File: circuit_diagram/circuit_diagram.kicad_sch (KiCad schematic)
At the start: 8 parts, among them J1 GPIO, J2 OLED_I2C_display, SW1 Hall_Effect_Flow_Switch, U1 MCP3008, U2 40PC250G

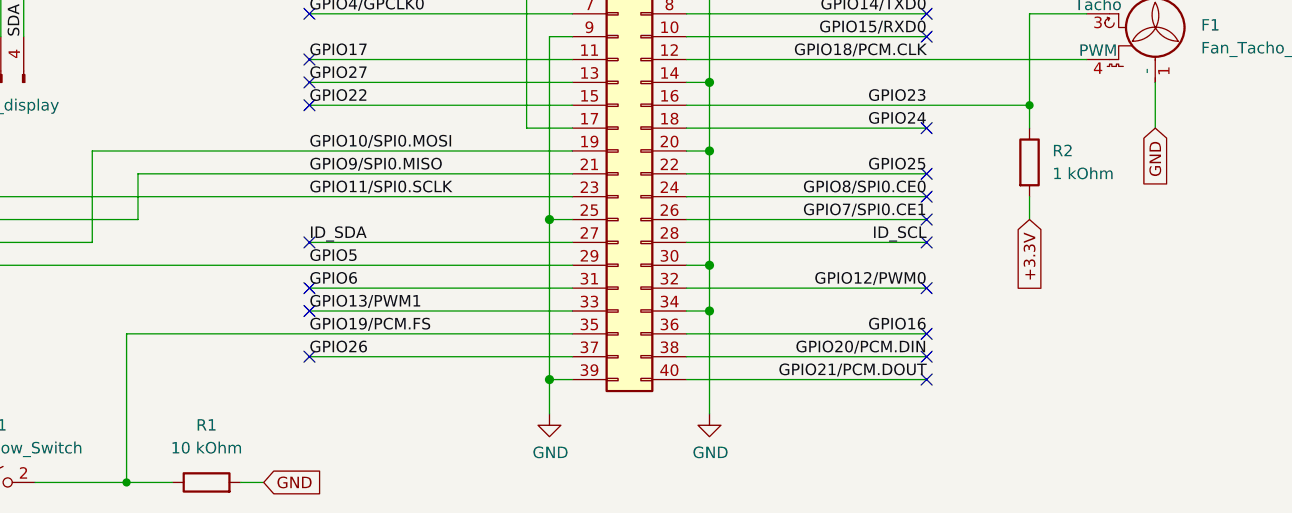
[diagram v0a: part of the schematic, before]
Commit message: Change to kΩ from kOhm
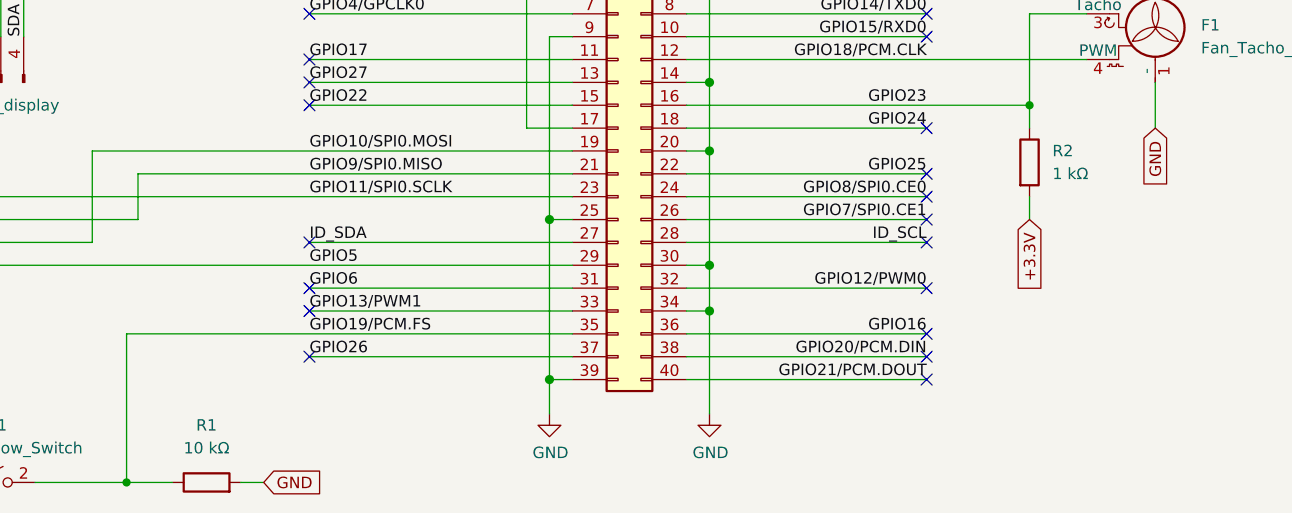
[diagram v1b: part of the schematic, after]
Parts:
- R1: value 10 kOhm -> 10 kΩ
- R2: value 1 kOhm -> 1 kΩ
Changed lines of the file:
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@@
       (effects (font (size 1.27 1.27)) (justify left))
     )
-    (property "Value" "1 kOhm" (at 228.6 106.68 0)
+    (property "Value" "1 kΩ" (at 228.6 106.68 0)
       (effects (font (size 1.27 1.27)) (justify left))
     )
@@
       (effects (font (size 1.27 1.27)))
     )
-    (property "Value" "10 kOhm" (at 134.62 137.16 90)
+    (property "Value" "10 kΩ" (at 134.62 137.16 90)
       (effects (font (size 1.27 1.27)))
     )

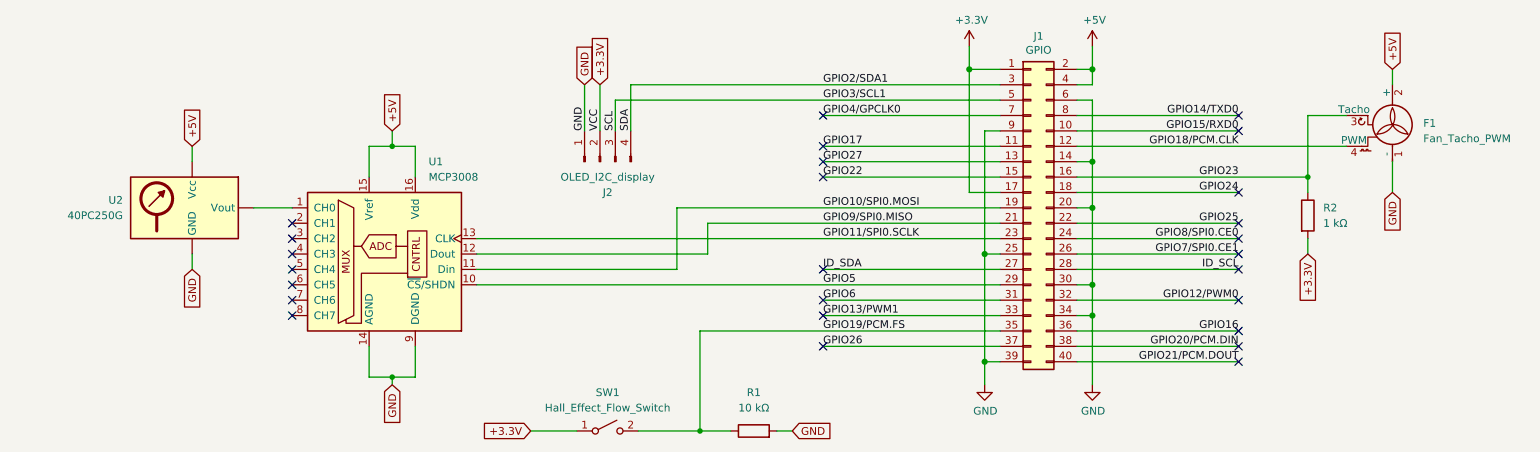
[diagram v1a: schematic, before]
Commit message: Improve Documentation (#27)
* Try relative link to mp4

* Revert relative path

* Try relative jpg

* Fix typo

* Test table of images

* Table formatting

* link all jpg

* Rename

* Fix typo

* Final touches on circuit diagram
Save pdf and svg

* Update README for circuit diagram

* edit README

* Update svg

* update README

* Change link style

* Updated README

* Added markdownlint

* Lint markdown files

* Update linters to match `pre-commit autoupdate` changes
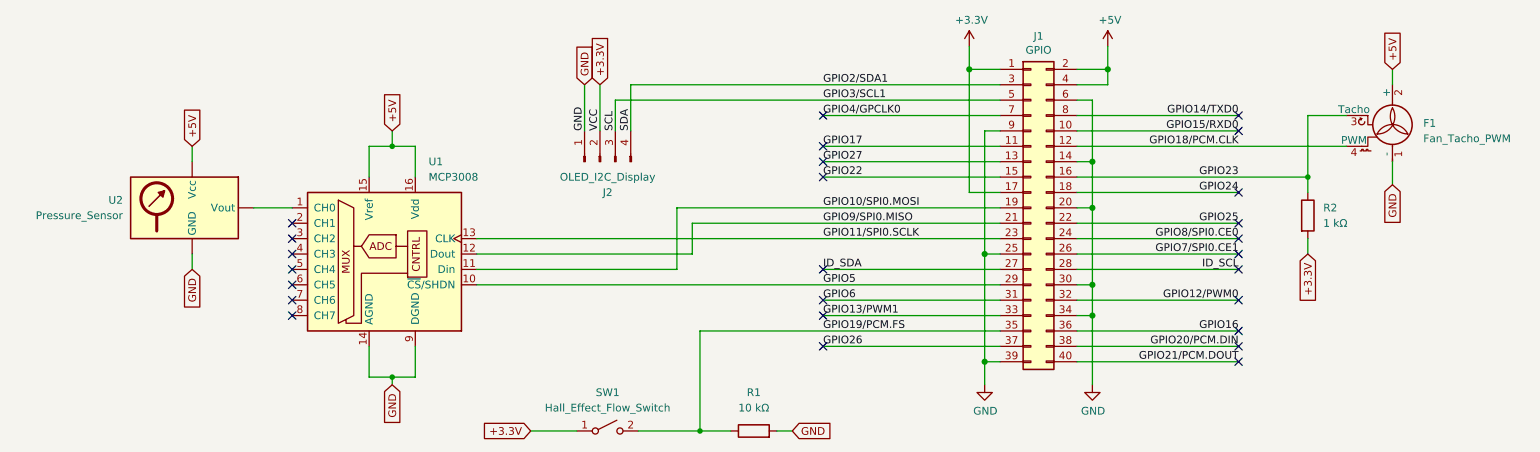
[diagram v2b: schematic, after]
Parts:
- J2: value OLED_I2C_display -> OLED_I2C_Display
- U2: value 40PC250G -> Pressure_Sensor
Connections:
- net GPIO10/SPI0.MOSI renamed  GPIO10/SPI0.MOSI
- net GPIO11/SPI0.SCLK renamed  GPIO11/SPI0.SCLK
- net GPIO12/PWM0 renamed GPIO12/PWM0 
- net GPIO13/PWM1 renamed  GPIO13/PWM1
- net GPIO14/TXD0 renamed GPIO14/TXD0 
- net GPIO15/RXD0 renamed GPIO15/RXD0 
- net GPIO16 renamed GPIO16 
- net GPIO17 renamed  GPIO17
- net GPIO18/PCM.CLK renamed GPIO18/PCM.CLK 
- net GPIO19/PCM.FS renamed  GPIO19/PCM.FS
- net GPIO20/PCM.DIN renamed GPIO20/PCM.DIN 
- net GPIO21/PCM.DOUT renamed GPIO21/PCM.DOUT 
- net GPIO22 renamed  GPIO22
- net GPIO23 renamed GPIO23 
- net GPIO24 renamed GPIO24 
- net GPIO25 renamed GPIO25 
- net GPIO26 renamed  GPIO26
- net GPIO27 renamed  GPIO27
- net GPIO2/SDA1 renamed  GPIO2/SDA1
- net GPIO3/SCL1 renamed  GPIO3/SCL1
- net GPIO4/GPCLK0 renamed  GPIO4/GPCLK0
- net GPIO5 renamed  GPIO5
- net GPIO6 renamed  GPIO6
- net GPIO7/SPI0.CE1 renamed GPIO7/SPI0.CE1 
- net GPIO8/SPI0.CE0 renamed GPIO8/SPI0.CE0 
- net GPIO9/SPI0.MISO renamed  GPIO9/SPI0.MISO
- net ID_SCL renamed ID_SCL 
- net ID_SDA renamed  ID_SDA
